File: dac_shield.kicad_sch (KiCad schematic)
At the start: 27 parts

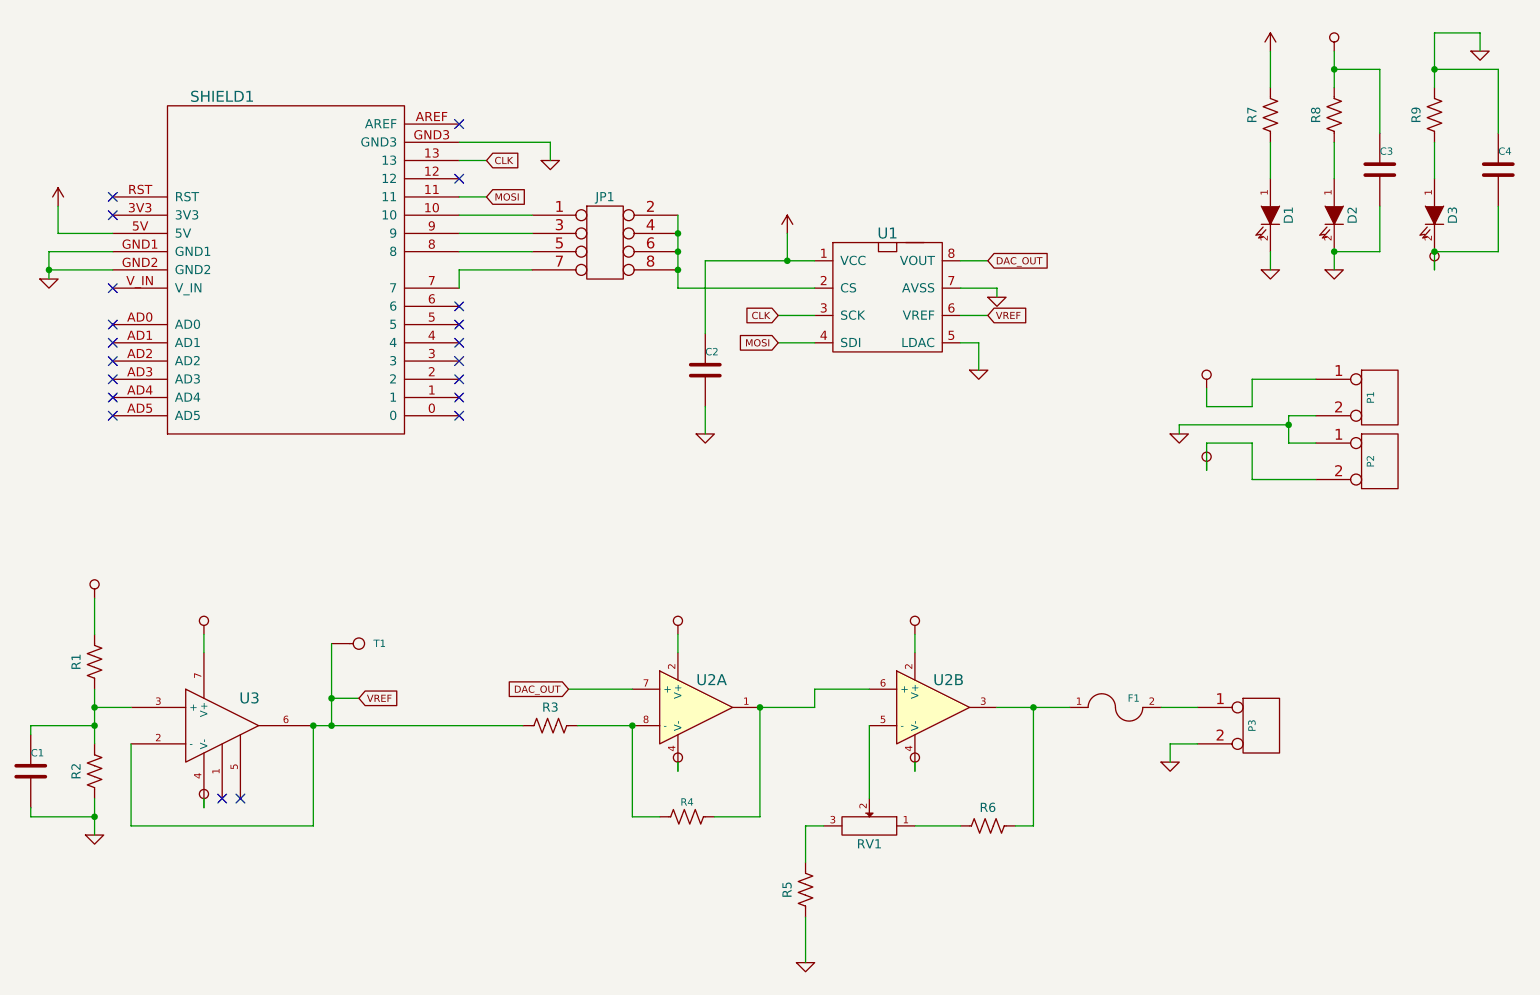
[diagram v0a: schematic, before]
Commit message: Updated all power symbols
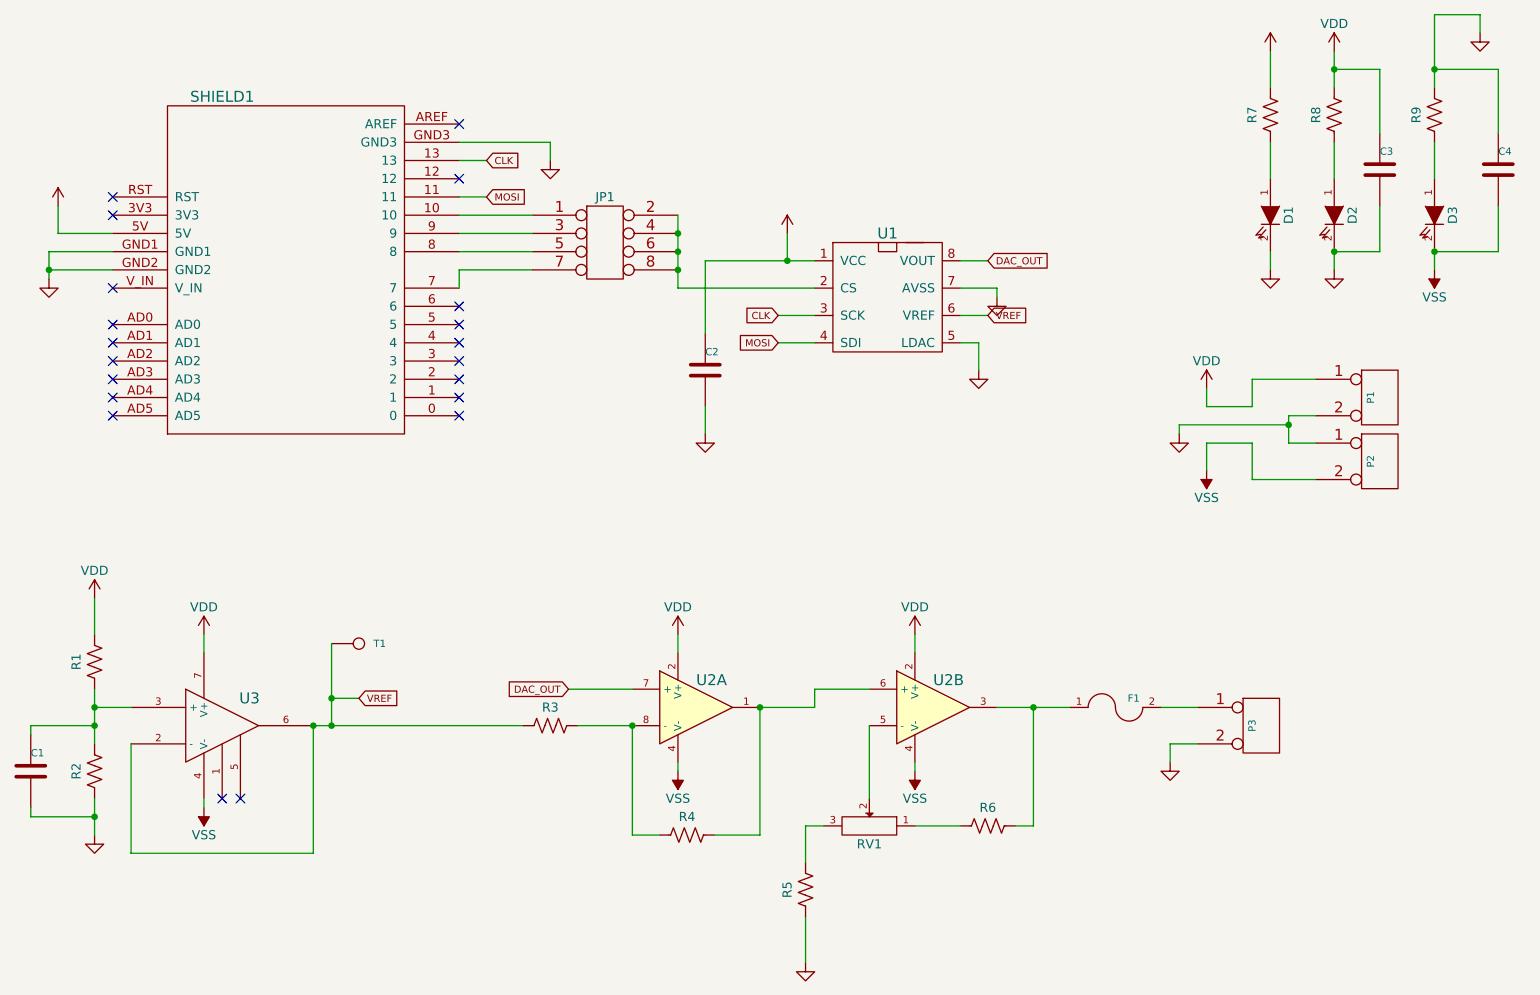
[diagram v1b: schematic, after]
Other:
- moved on the sheet: R4

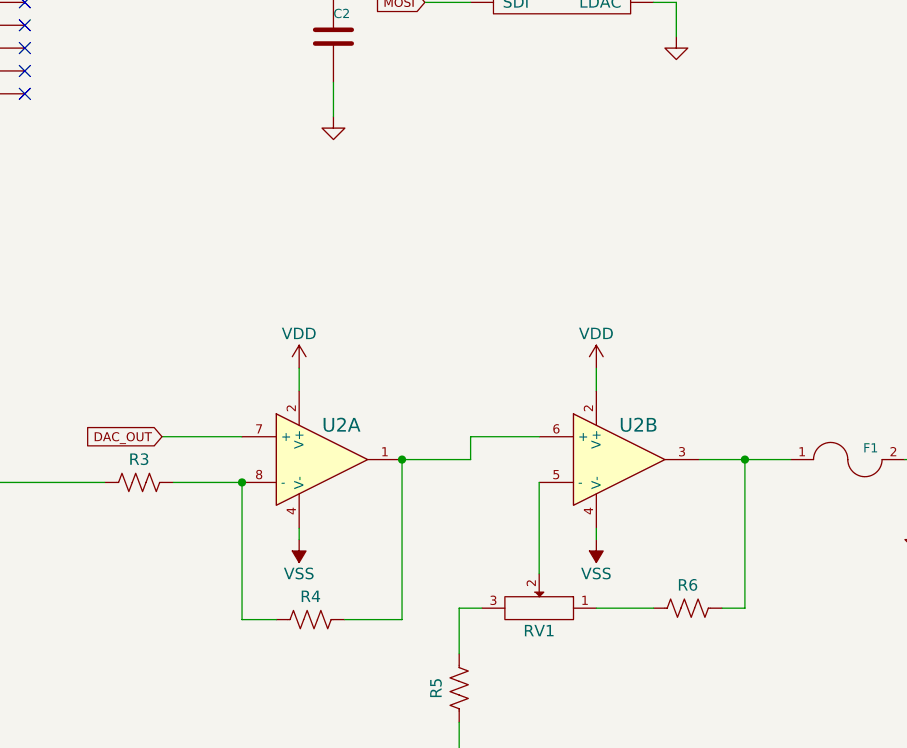
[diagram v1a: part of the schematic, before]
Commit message: Changed symbol for TCA0372
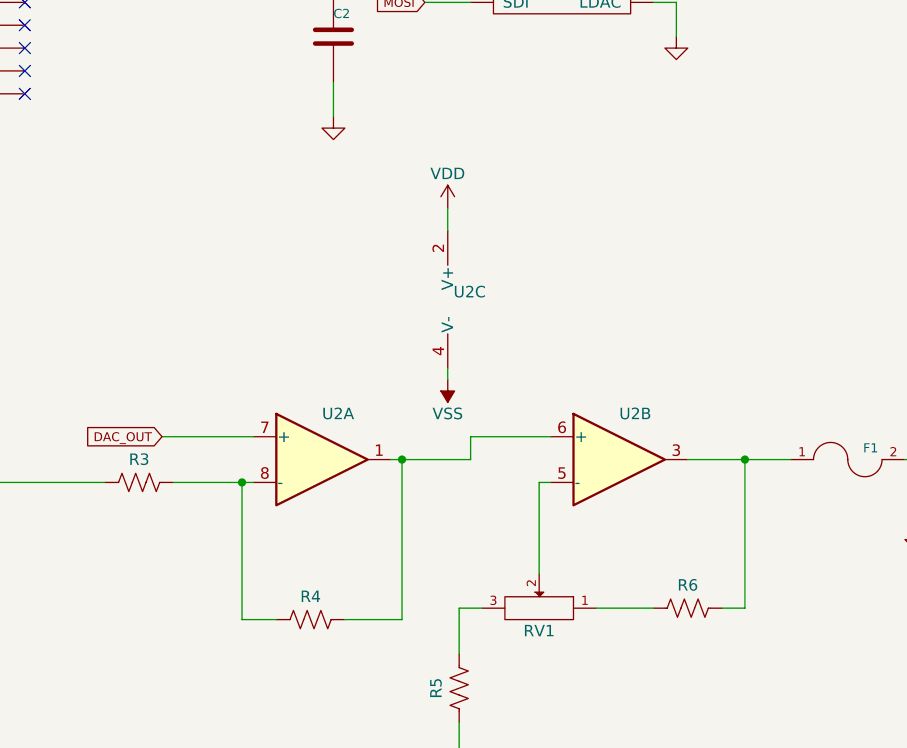
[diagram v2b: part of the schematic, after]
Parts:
- added unit 3 of U2
- U2: symbol dac_shield-rescue:TCA0372 -> Amplifier_Operational:L272M
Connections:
- net VDD: now also U2.2 (V+); no longer U2.2 (V+), U2.2 (V+)
- net VSS: now also U2.4 (V-); no longer U2.4 (V-), U2.4 (V-)

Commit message: Created custom-symbols to copy symbols with no replacement
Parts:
- SHIELD1: symbol dac_shield-rescue:ARDUINO_SHIELD -> custom-symbols:ARDUINO_SHIELD
- U1: symbol dac_shield-rescue:MCP4921 -> custom-symbols:MCP4921
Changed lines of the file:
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@@
     )
   )
-  (symbol (lib_id "dac_shield-rescue:ARDUINO_SHIELD") (at 62.23 54.61 0) (unit 1)
+  (symbol (lib_id "custom-symbols:ARDUINO_SHIELD") (at 62.23 54.61 0) (unit 1)
     (in_bom yes) (on_board yes)
     (property "Reference" "SHIELD1" (id 0) (at 53.34 30.48 0)
@@
     (pin "1")
   )
-  (symbol (lib_id "dac_shield-rescue:MCP4921") (at 146.05 58.42 0) (unit 1)
+  (symbol (lib_id "custom-symbols:MCP4921") (at 146.05 58.42 0) (unit 1)
     (in_bom yes) (on_board yes)
     (property "Reference" "U1" (id 0) (at 146.05 49.53 0)

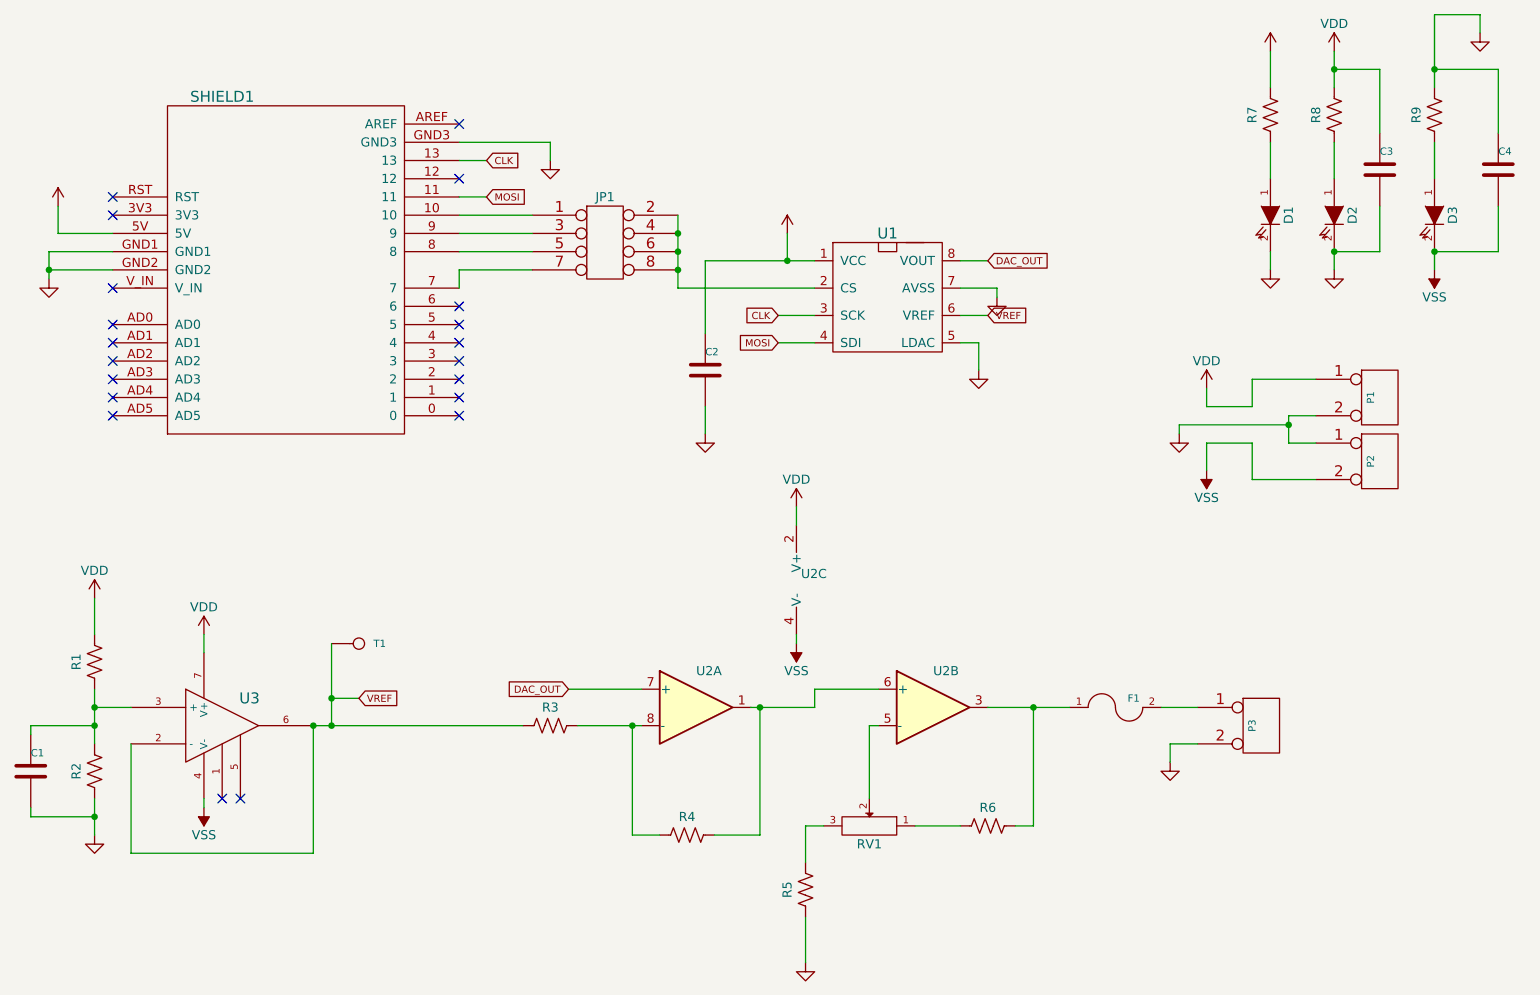
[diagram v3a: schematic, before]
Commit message: Removed all rescue symbols
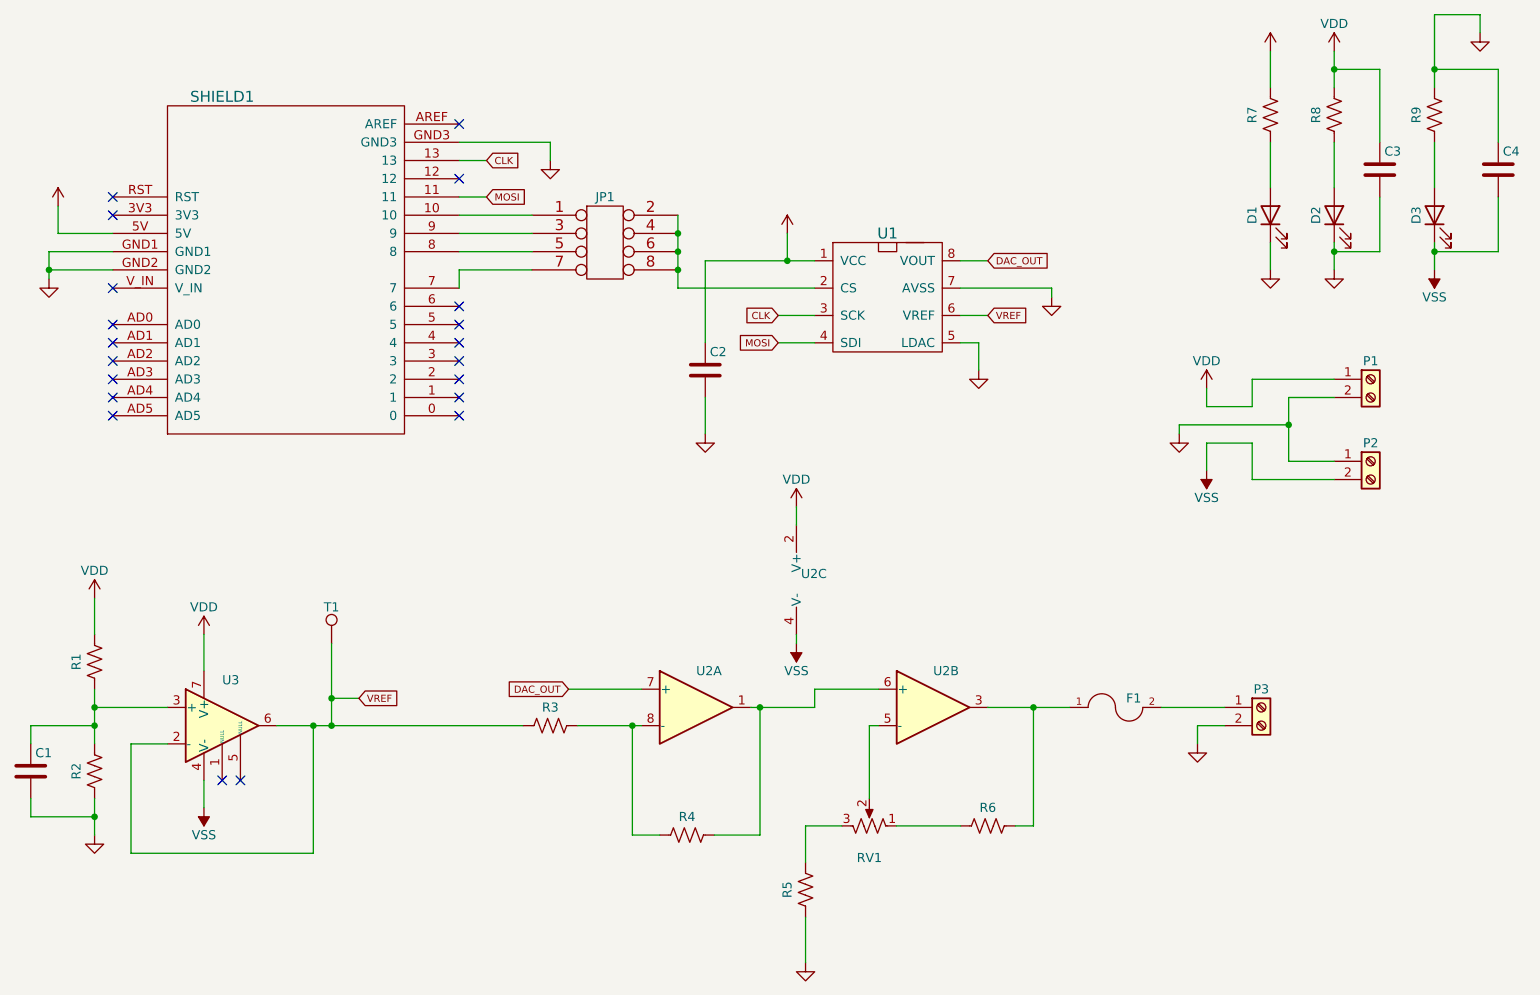
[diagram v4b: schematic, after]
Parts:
- C1, C2, C3, C4: symbol dac_shield-rescue:C-RESCUE-dac_shield -> Device:C
- D1, D2, D3: symbol dac_shield-rescue:LED-RESCUE-dac_shield -> Device:LED
- F1: symbol dac_shield-rescue:FUSE -> custom-symbols:FUSE
- JP1: symbol dac_shield-rescue:CONN_4X2 -> custom-symbols:CONN_4X2
- P1, P2, P3: symbol dac_shield-rescue:CONN_2 -> Connector:Screw_Terminal_01x02
- RV1: symbol dac_shield-rescue:POT -> Device:R_Potentiometer_US
- T1: symbol dac_shield-rescue:CONN_1 -> Connector:TestPoint
- U3: symbol dac_shield-rescue:LM741-RESCUE-dac_shield -> Amplifier_Operational:LM741
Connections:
- net GND: now also D1.1 (K), D2.1 (K); no longer D1.2 (K), D2.2 (K)
- net VSS: now also D3.1 (K); no longer D3.2 (K)
- net at R7.1: now also D1.2 (A); no longer D1.1 (A)
- net at R8.1: now also D2.2 (A); no longer D2.1 (A)
- net at R9.1: now also D3.2 (A); no longer D3.1 (A)

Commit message: Re-mapping symbols to footprints
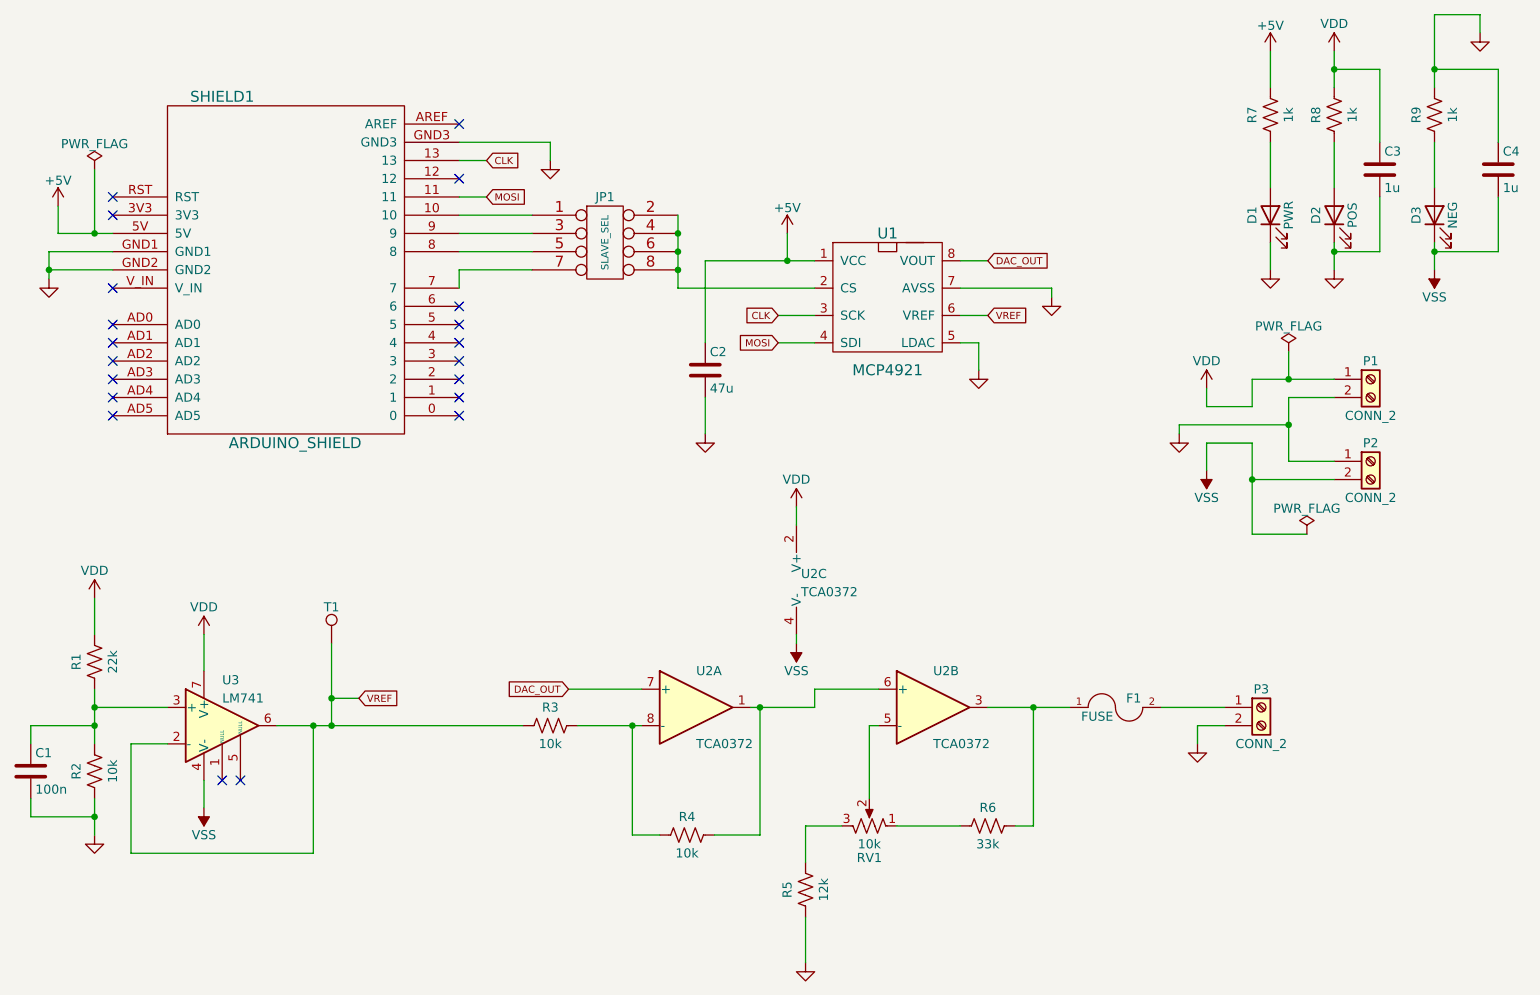
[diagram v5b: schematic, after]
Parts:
- C1: value (none) -> 100n; footprint (none) -> custom-footprints:SM1206_VIS
- C2: value (none) -> 47u; footprint (none) -> custom-footprints:SM1206POL_VIS
- C3, C4: value (none) -> 1u; footprint (none) -> custom-footprints:SM1206_VIS
- D1: value (none) -> PWR
- D2: value (none) -> POS
- D3: value (none) -> NEG
- F1: value (none) -> FUSE; footprint (none) -> custom-footprints:SM1210L
- JP1: value (none) -> SLAVE_SEL; footprint (none) -> custom-footprints:pin_array_4x2
- P1, P2, P3: value (none) -> CONN_2; footprint (none) -> custom-footprints:bornier2
- R1: value (none) -> 22k; footprint (none) -> custom-footprints:SM0603_VIS
- R2, R3, R4: value (none) -> 10k; footprint (none) -> custom-footprints:SM0603_VIS
- R5: value (none) -> 12k; footprint (none) -> custom-footprints:SM0603_VIS
- R6: value (none) -> 33k; footprint (none) -> custom-footprints:SM0603_VIS
- R7, R8, R9: value (none) -> 1k; footprint (none) -> custom-footprints:SM0603_VIS
- RV1: value (none) -> 10k; footprint (none) -> custom-footprints:Var_resistor
- SHIELD1: value (none) -> ARDUINO_SHIELD; footprint (none) -> custom-footprints:ARDUINO_SHIELD_2_040pins
- T1: value (none) -> VrefTest; footprint (none) -> custom-footprints:PINTST
- U1: value (none) -> MCP4921; footprint (none) -> custom-footprints:DIP-8__300_ELL
- U2: value (none) -> TCA0372; footprint (none) -> custom-footprints:DIP-8__300_ELL
- U3: value (none) -> LM741; footprint (none) -> custom-footprints:DIP-8__300_ELL
